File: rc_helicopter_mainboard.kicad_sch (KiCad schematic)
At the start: 20 parts, among them J1 Battery Pack, J2 SWD, J3 Main Connector, SW1 Tactswitch, U1 STM32L4P5RET6, Y1 16MHz

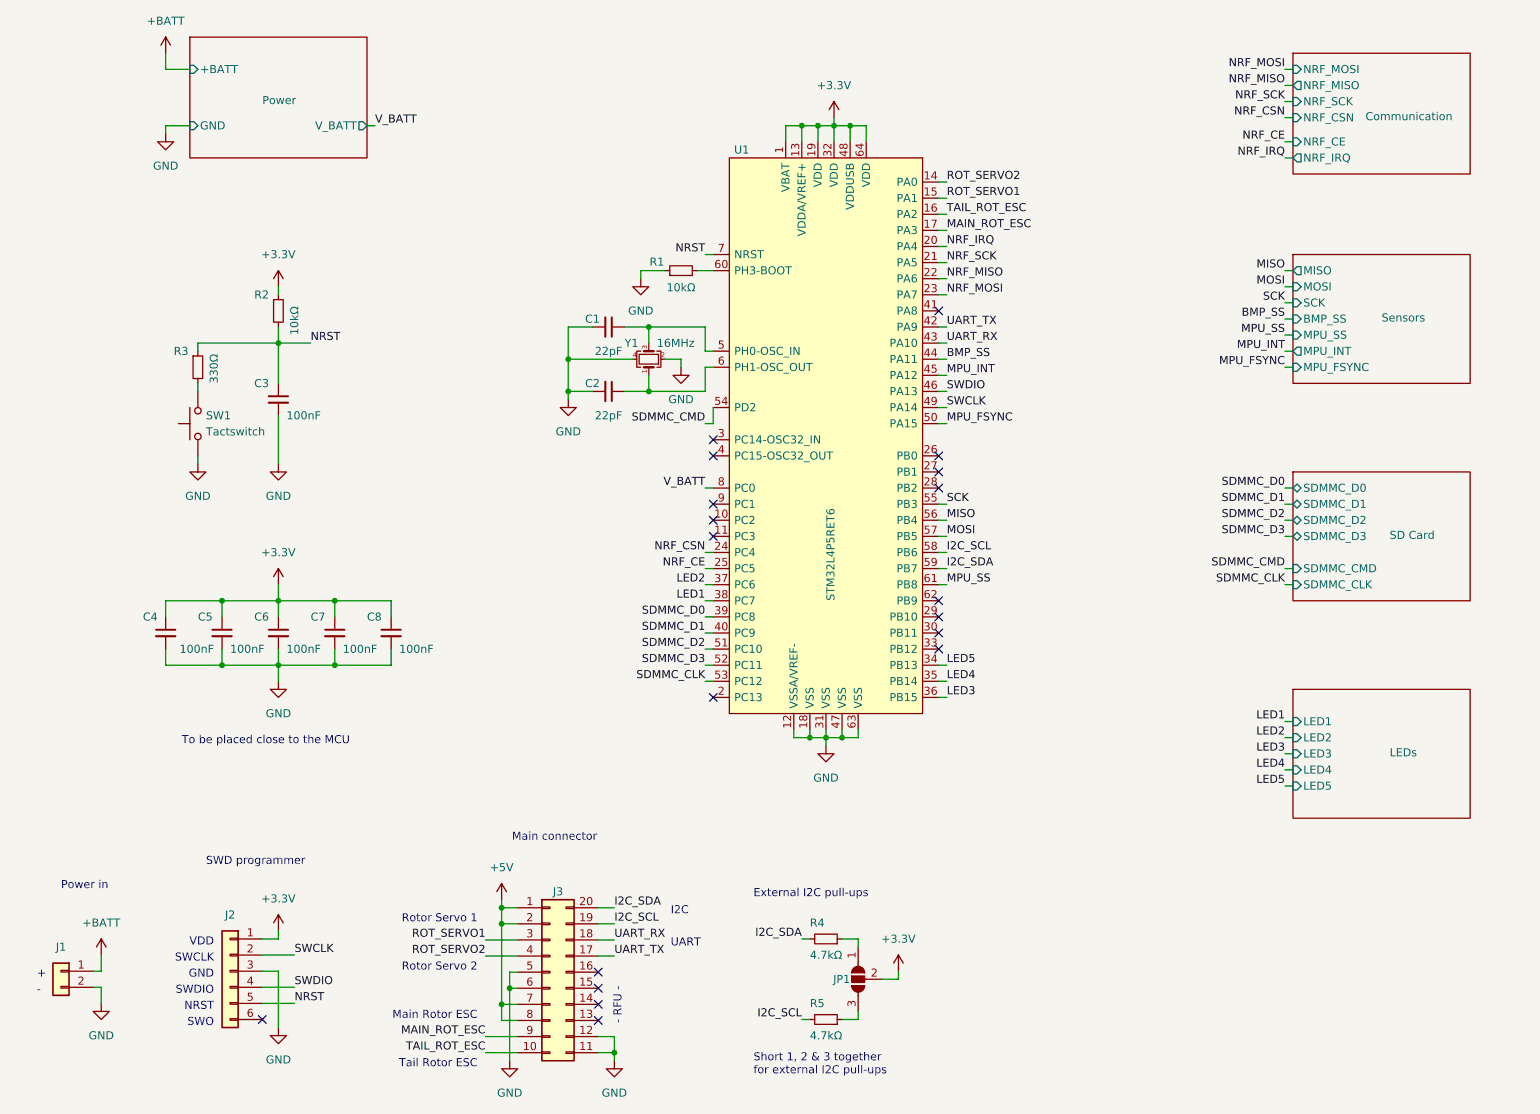
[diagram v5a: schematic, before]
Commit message: Route PCB tracks
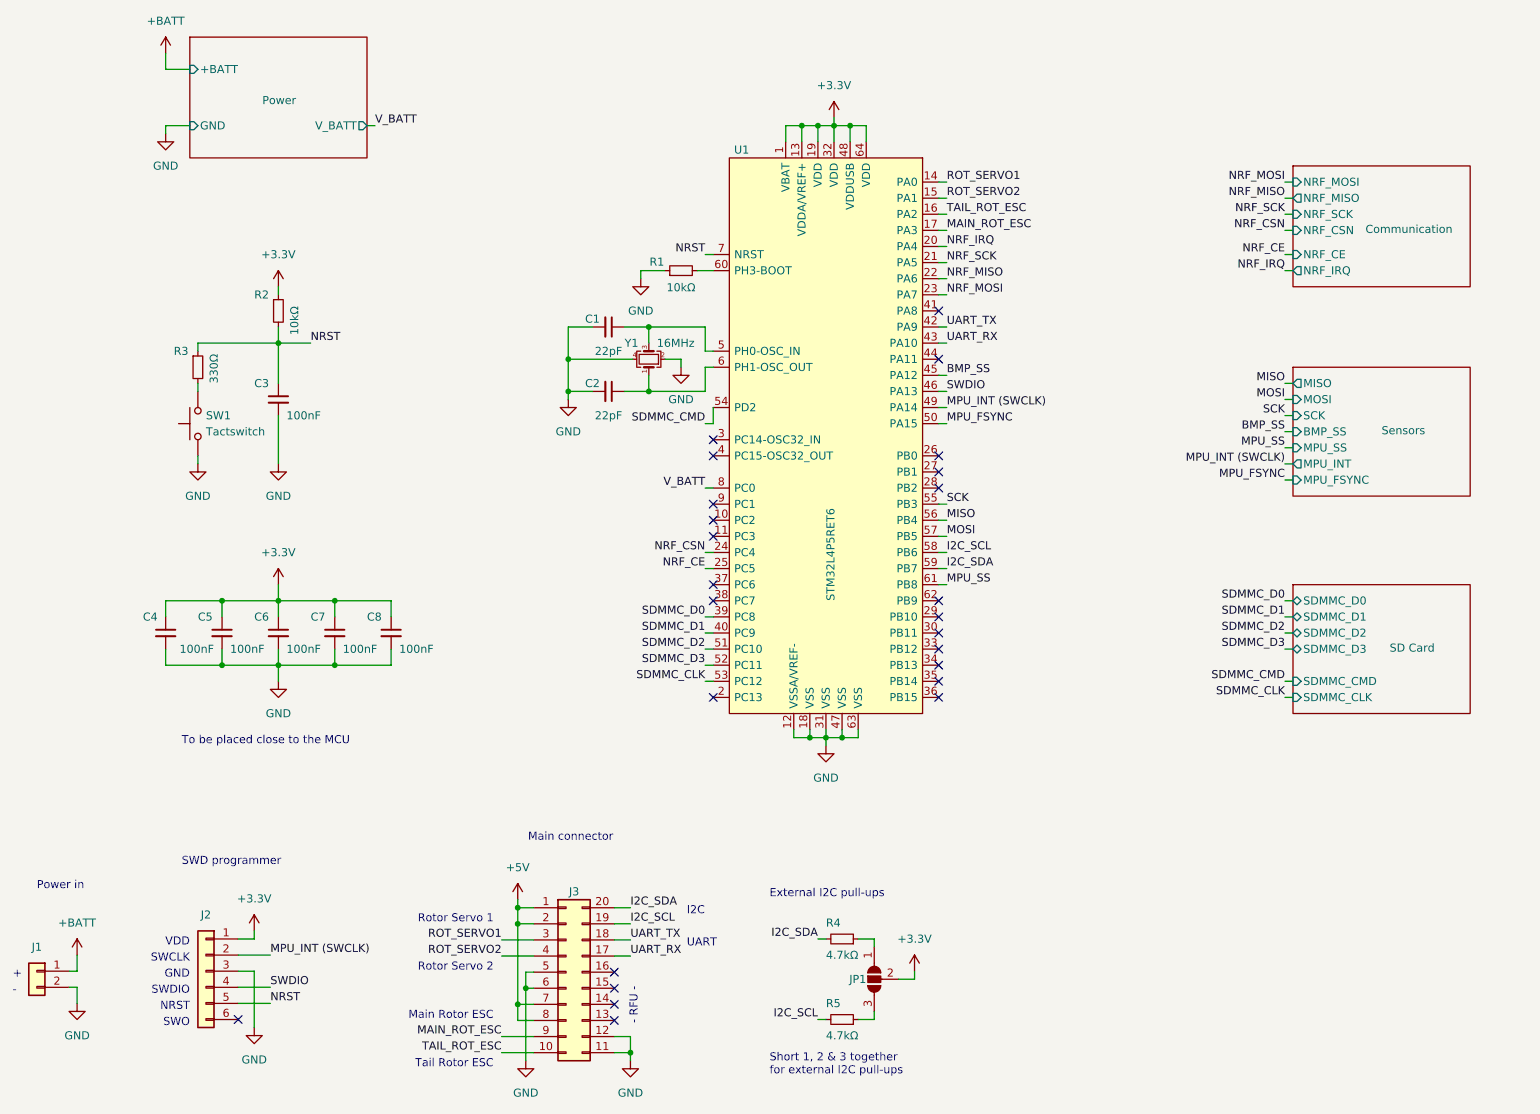
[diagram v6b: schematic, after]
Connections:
- net MPU_INT is gone; now on net BMP_SS: U1.45 (PA12)
- net BMP_SS: no longer U1.44 (PA11)
- net ROT_SERVO1: now also U1.14 (PA0); no longer U1.15 (PA1)
- net ROT_SERVO2: now also U1.15 (PA1); no longer U1.14 (PA0)
- net UART_RX: now also J3.17 (Pin_17); no longer J3.18 (Pin_18)
- net UART_TX: now also J3.18 (Pin_18); no longer J3.17 (Pin_17)
- net LED1: no longer names the net of U1.38 (PC7)
- net LED2: no longer names the net of U1.37 (PC6)
- net LED3: no longer names the net of U1.36 (PB15)
- net LED4: no longer names the net of U1.35 (PB14)
- net LED5: no longer names the net of U1.34 (PB13)
- net SWCLK renamed MPU_INT (SWCLK)
- no-connect marks 19 -> 25
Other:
- removed sheet LEDs
- moved on the sheet: J1, J2, J3, JP1, R4, R5
